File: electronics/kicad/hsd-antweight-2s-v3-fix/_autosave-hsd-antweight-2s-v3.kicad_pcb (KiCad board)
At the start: 2 copper layers, 78 x 56 mm, 10 parts, among them J10 5V(3.7-5V) GND VLIPO, J4 BATTERY, J5 MOTOR LEFT, J6 MOTOR RIGHT, SW1 SW EXT VBAT_RAW/VBAT_SW, U1 ESP32-C3 SUPERMINI, U2 DRV8833, U3 EXT REG LOGIC VIN GND VOUT

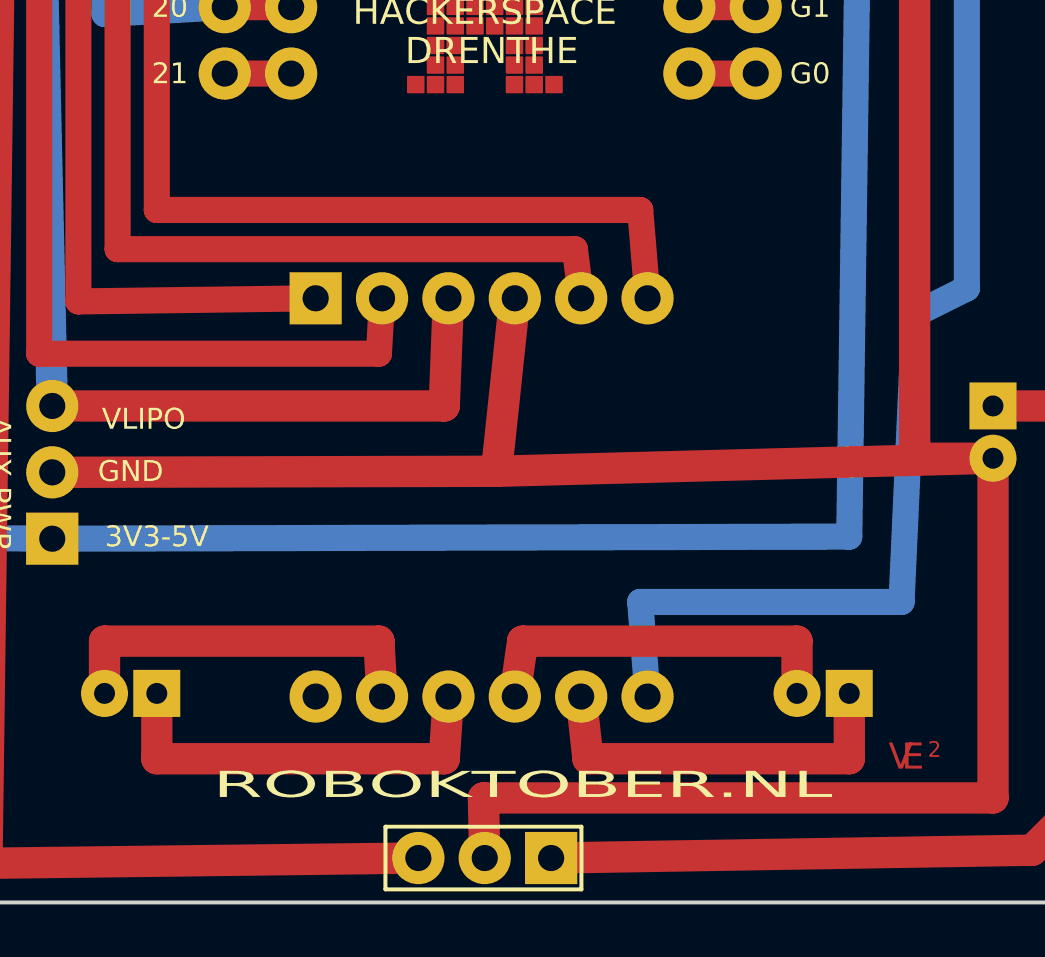
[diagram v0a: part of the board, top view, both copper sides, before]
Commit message: Align Wallie design notes with 1S default power architecture
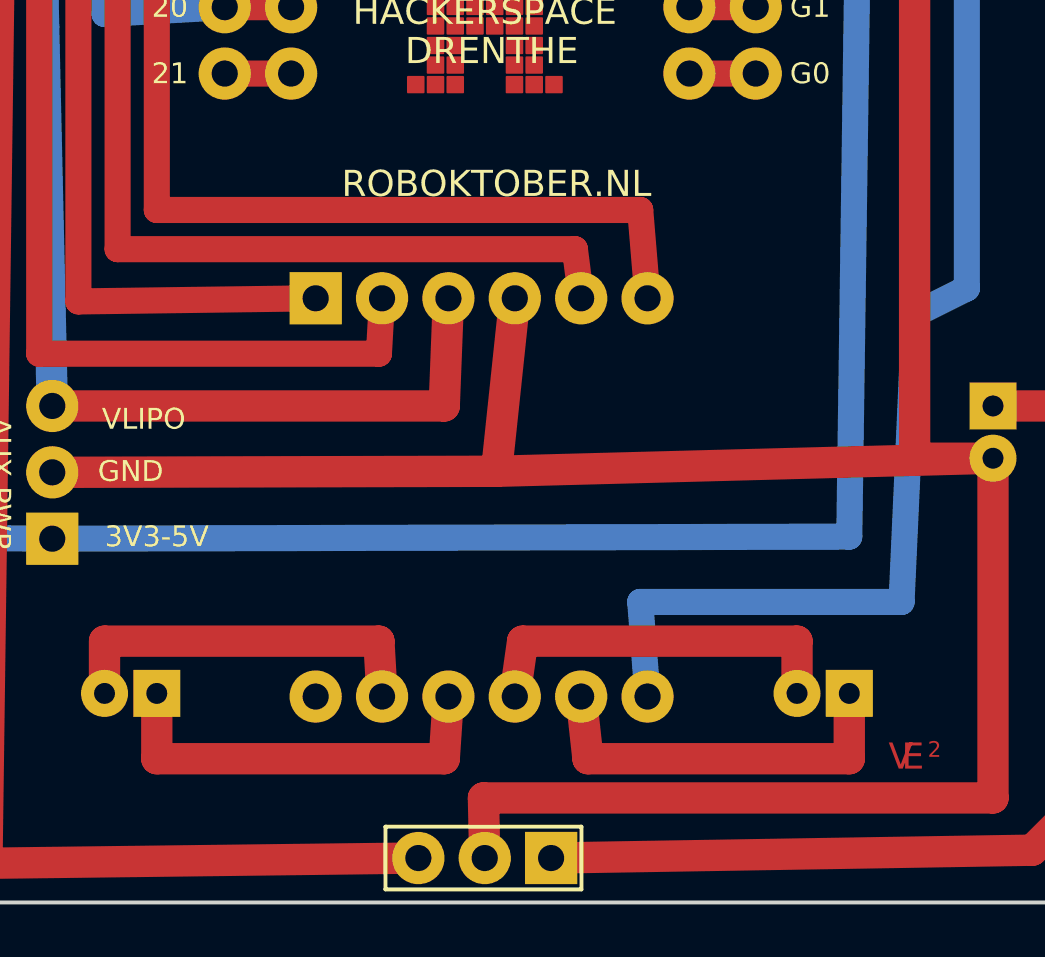
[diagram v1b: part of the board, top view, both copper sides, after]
